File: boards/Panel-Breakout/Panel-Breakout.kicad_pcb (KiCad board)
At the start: 2 copper layers, 74.9 x 52.7 mm, 18 parts, among them J1 Raspberry_Pi_2_3, J2 BoardCon, J3 PanelLeft, J4 PanelRight, U1 ICL3232

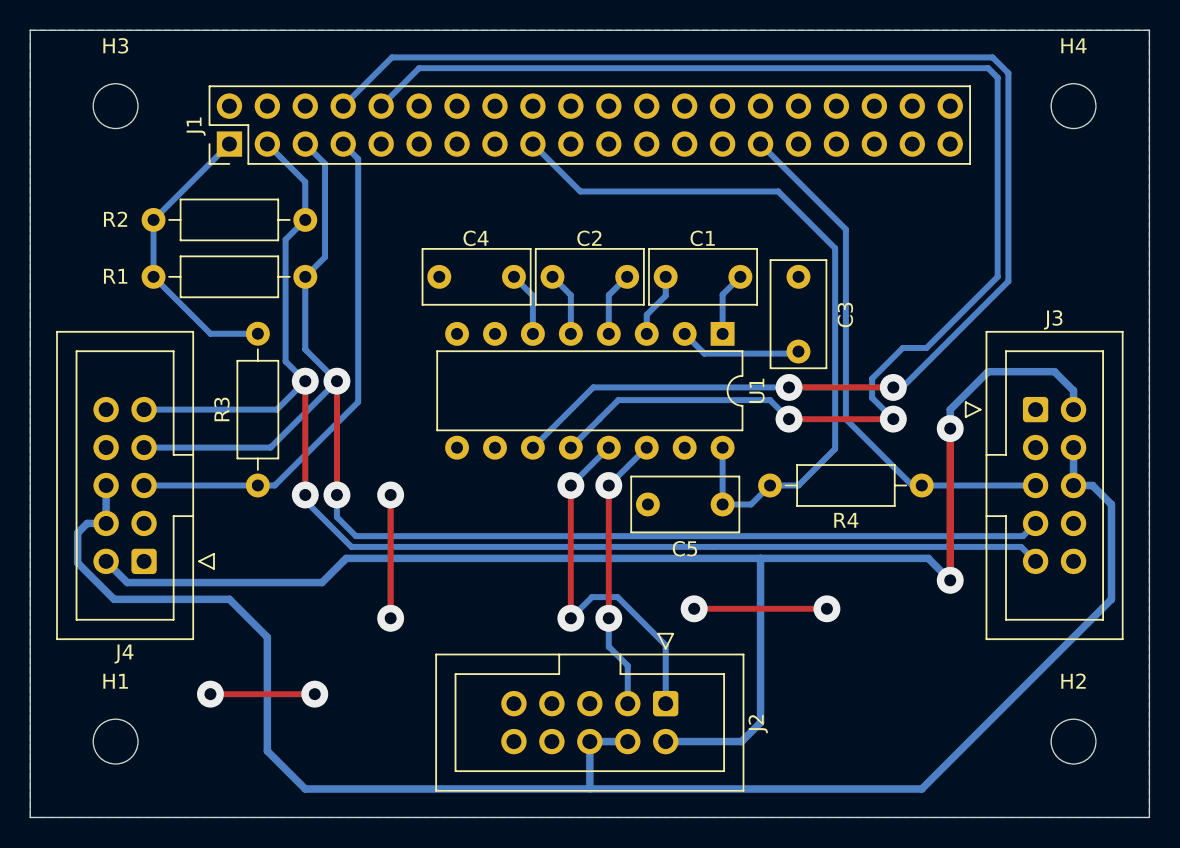
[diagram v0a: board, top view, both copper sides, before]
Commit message: Updated panel breakout board to use second I2C to avoid conflict with display
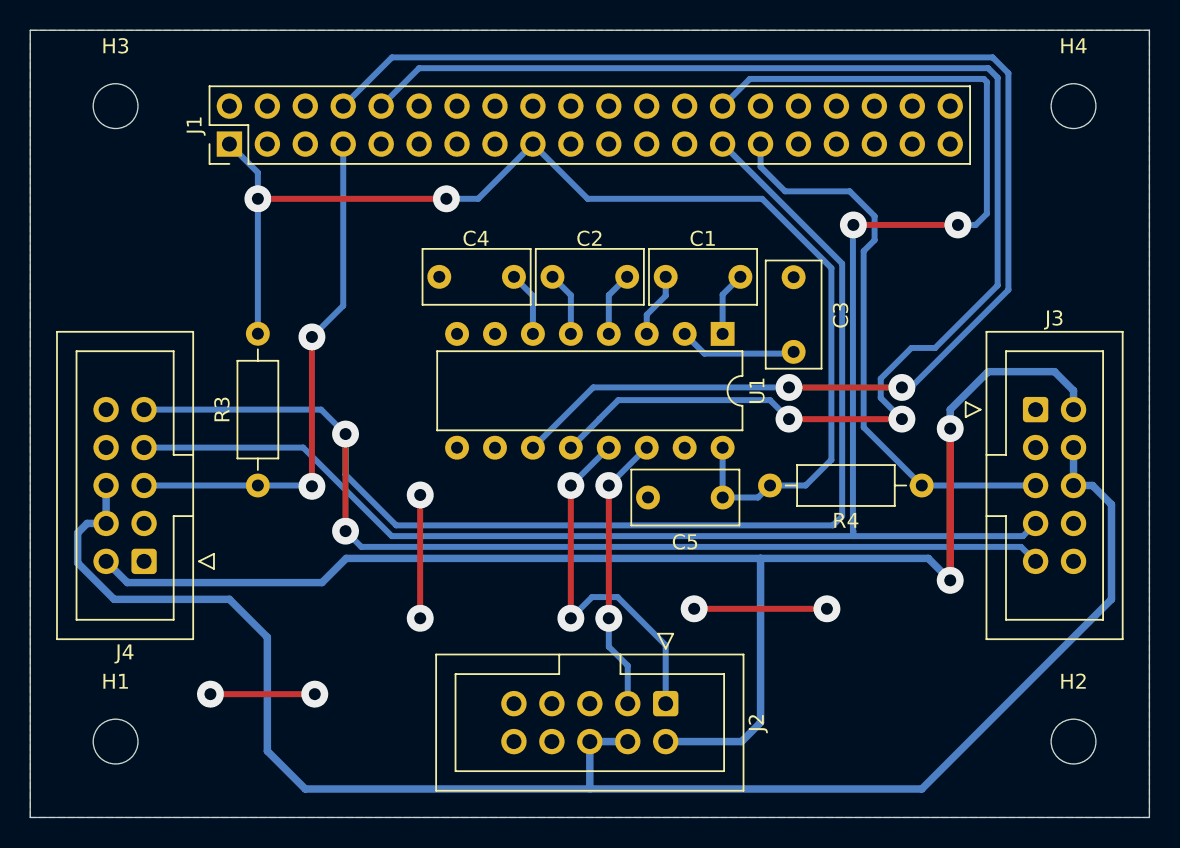
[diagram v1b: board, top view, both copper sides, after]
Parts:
- removed R1, R2: 1k8, Resistor_THT:R_Axial_DIN0207_L6.3mm_D2.5mm_P10.16mm_Horizontal
- moved C5 0.47 mm to (150.5, 100.5)
- moved C3 0.33 mm to (155.2, 90.8)
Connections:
- J1 pad 27: unconnected-(J1-ID_SD/GPIO0-Pad27) -> /SDA
- J1 pad 28: unconnected-(J1-ID_SC/GPIO1-Pad28) -> /SCL
- J1 pad 3: /SDA -> unconnected-(J1-SDA/GPIO2-Pad3)
- J1 pad 5: /SCL -> unconnected-(J1-SCL/GPIO3-Pad5)
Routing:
- net /SDA: track 88.2 -> 133.6 mm
- net /SCL: track 89.4 -> 120.0 mm
- net +3.3V: track 69.0 -> 81.8 mm, vias 0 -> 2
- net /IntLeft: track 35.3 -> 38.7 mm
- net /IntRight: track 34.3 -> 35.0 mm, vias 0 -> 2

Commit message: Fixed missing I2C pullup for Raspberry I2C-0
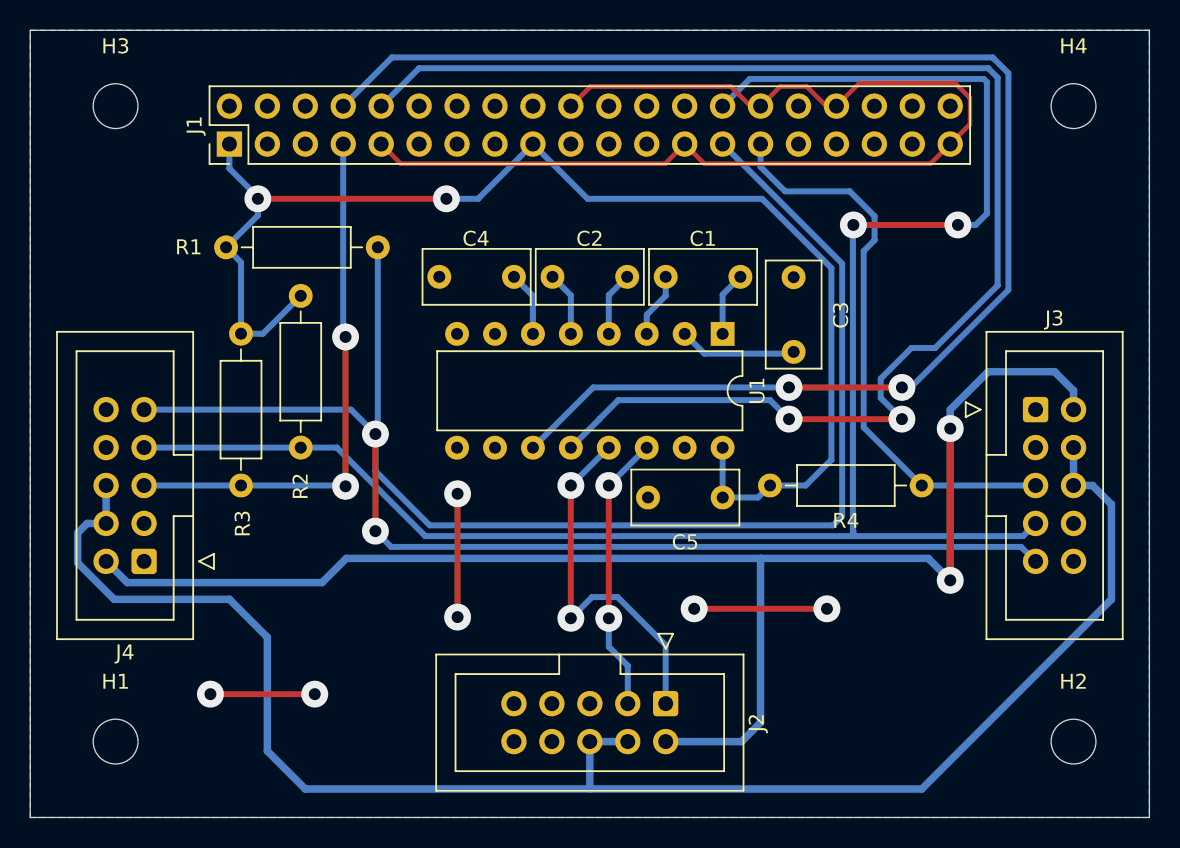
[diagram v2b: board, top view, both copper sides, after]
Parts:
- added R1: 2.2k, Resistor_THT:R_Axial_DIN0207_L6.3mm_D2.5mm_P10.16mm_Horizontal, F.Cu at (127.4, 83.8)
- added R2: 2.2k, Resistor_THT:R_Axial_DIN0207_L6.3mm_D2.5mm_P10.16mm_Horizontal, F.Cu at (122.2, 97.2)
- moved R3 1.13 mm to (118.2, 99.7)
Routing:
- net GND: track 24.1 -> 98.0 mm
- net /SDA: track 133.6 -> 144.0 mm
- net +3.3V: track 81.8 -> 88.2 mm
- net /IntRight: track 35.0 -> 36.5 mm
